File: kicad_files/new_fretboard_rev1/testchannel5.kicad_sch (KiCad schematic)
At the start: 22 parts, among them U2 LX3302AQPW-TR-EASY

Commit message: got 6 of em
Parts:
- removed C12, C13: 680pf, Capacitor_SMD:C_0603_1608Metric, symbol Device:C
- removed C14, C15: 10pf, Capacitor_SMD:C_0402_1005Metric, symbol Device:C
- removed C16: 1uf, Capacitor_SMD:C_0603_1608Metric, symbol Device:C
- removed C17, C20: 100nf, Capacitor_SMD:C_0402_1005Metric, symbol Device:C
- removed C18, C19: 6.8nf, Capacitor_SMD:C_0402_1005Metric, symbol Device:C
- removed C21: 1000pf, Capacitor_SMD:C_0402_1005Metric, symbol Device:C
- removed C22: 470nf, Capacitor_SMD:C_0402_1005Metric, symbol Device:C
- removed L5, L6, L7, L8: L, NetTie:NetTie-2_SMD_Pad0.5mm, symbol Device:L
- removed R10, R11, R8, R9: 10R, Resistor_SMD:R_0402_1005Metric, symbol Device:R
- removed R12: 221R, Resistor_SMD:R_0402_1005Metric, symbol Device:R
- removed R13: 4.7R, Resistor_SMD:R_0402_1005Metric, symbol Device:R
- removed U2: LX3302AQPW-TR-EASY, Snapeda:14-TSSOP_MCH-L, symbol Snapeda:LX3302AQPW-TR-EASY
- added C56, C62: 100nf, Capacitor_SMD:C_0402_1005Metric, symbol Device:C
- added C57: 1000pf, Capacitor_SMD:C_0402_1005Metric, symbol Device:C
- added C58: 470nf, Capacitor_SMD:C_0402_1005Metric, symbol Device:C
- added C59: 1uf, Capacitor_SMD:C_0603_1608Metric, symbol Device:C
- added C60, C61: 6.8nf, Capacitor_SMD:C_0402_1005Metric, symbol Device:C
- added C63, C64: 10pf, Capacitor_SMD:C_0402_1005Metric, symbol Device:C
- added C65, C66: 680pf, Capacitor_SMD:C_0603_1608Metric, symbol Device:C
- added L21, L22, L23, L24: L, NetTie:NetTie-2_SMD_Pad0.5mm, symbol Device:L
- added R31: 4.7R, Resistor_SMD:R_0402_1005Metric, symbol Device:R
- added R32: 221R, Resistor_SMD:R_0402_1005Metric, symbol Device:R
- added R33, R34, R35, R36: 10R, Resistor_SMD:R_0402_1005Metric, symbol Device:R
- added U6: LX3302AQPW-TR-EASY, Snapeda:14-TSSOP_MCH-L, symbol Snapeda:LX3302AQPW-TR-EASY
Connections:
- net CL1B_A: now also L24.1, R36.2
- net CL1_A: now also C63.1, R36.1, U6.8 (CL1)
- net CL2B_A: now also L23.1, R35.2
- net CL2_A: now also C64.1, R35.1, U6.10 (CL2)
- net GND: now also C56.1, C57.1, C58.1, C59.1, C60.1, C61.1, C63.2, C64.2, C65.2, C66.2, L23.2, L24.2, U6.2 (GND), U6.9 (GNDCL)
- net OSC11_A: now also C65.1, L21.2, U6.13 (OSC1)
- net OSC12_A: now also C66.1, L22.2, U6.12 (OSC2)
- net SUB_A: now also C62.1, U6.11 (SUB)
- net VIN_A: now also C57.2, C58.2, R31.1, R33.2, R34.1, U6.4 (VIN)
- new net: C60.2, R32.2
- new net: C61.2, R32.1, R33.1, U6.6 (IO2)
- new net: C56.2, R31.2
- new net: C59.2, C62.2, U6.5 (VDD)
- new net /OSC2B_A: L21.1, L22.1, R34.2
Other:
- removed sheet testchannel1
- removed sheet testchannel2
- removed sheet testchannel3
- removed sheet testchannel4
- removed sheet testchannel5

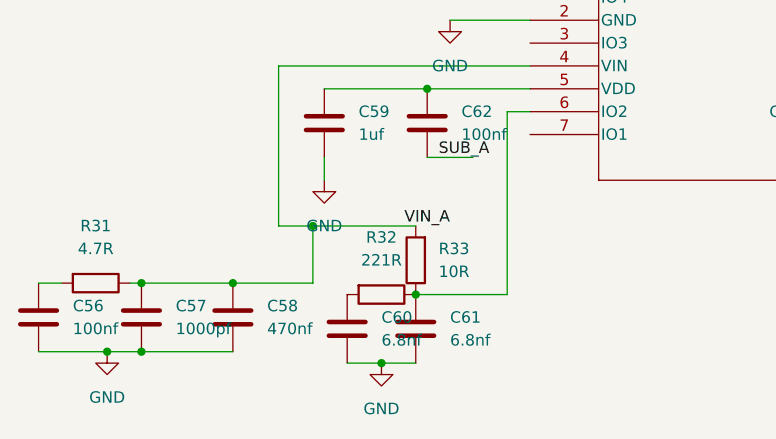
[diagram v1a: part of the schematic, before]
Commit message: stm32 micro added
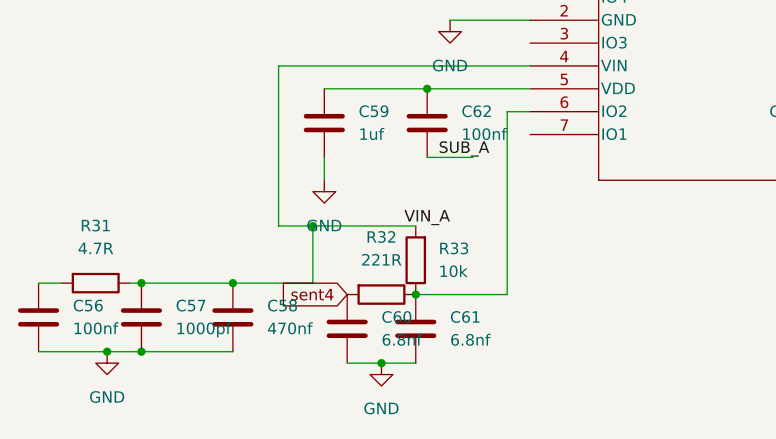
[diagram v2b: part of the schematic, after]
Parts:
- R33: value 10R -> 10k
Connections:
- net sent4: now reaches C60.2, R32.2
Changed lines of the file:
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@@
+		)
+	)
+	(global_label "sent4"
+		(shape input)
+		(at 110.49 125.73 180)
+		(fields_autoplaced yes)
+		(effects
+			(font
+				(size 1.27 1.27)
+			)
+			(justify right)
+		)
+		(property "Intersheetrefs" "${INTERSHEET_REFS}"
+			(at 102.3039 125.73 0)
+			(effects
+				(font
+					(size 1.27 1.27)
+				)
+				(justify right)
+				(hide yes)
+			)
 		)
 	)
@@
 			)
 		)
-		(property "Component Class" ""
-			(at 184.15 57.15 0)
-			(effects
-				(font
-					(size 1.27 1.27)
-				)
-				(hide yes)
-			)
-		)
 		(pin "2"
 		)
@@
 			)
 		)
-		(property "Component Class" ""
-			(at 203.2 121.92 90)
-			(effects
-				(font
-					(size 1.27 1.27)
-				)
-				(hide yes)
-			)
-		)
 		(pin "1"
 		)
@@
 			)
 		)
-		(property "Component Class" ""
-			(at 110.49 129.54 0)
-			(effects
-				(font
-					(size 1.27 1.27)
-				)
-				(hide yes)
-			)
-		)
 		(pin "1"
 		)
@@
 			)
 		)
-		(property "Value" "10R"
+		(property "Value" "10k"
 			(at 120.65 123.1899 0)
 			(effects
@@
 			)
 		)
-		(property "Component Class" ""
-			(at 118.11 121.92 0)
-			(effects
-				(font
-					(size 1.27 1.27)
-				)
-				(hide yes)
-			)
-		)
 		(pin "2"
 		)
@@
 			)
 		)
-		(property "Component Class" ""
-			(at 114.3 125.73 90)
-			(effects
-				(font
-					(size 1.27 1.27)
-				)
-				(hide yes)
-			)
-		)
 		(pin "2"
 		)
@@
 			)
 		)
-		(property "Component Class" ""
-			(at 204.47 85.09 90)
-			(effects
-				(font
-					(size 1.27 1.27)
-				)
-				(hide yes)
-			)
-		)
 		(pin "1"
 		)
@@
 			)
 		)
-		(property "Component Class" ""
-			(at 82.55 124.46 90)
-			(effects
-				(font
-					(size 1.27 1.27)
-				)
-				(hide yes)
-			)
-		)
 		(pin "2"
 		)
@@
 			)
 		)
-		(property "Component Class" ""
-			(at 194.31 68.58 0)
-			(effects
-				(font
-					(size 1.27 1.27)
-				)
-				(hide yes)
-			)
-		)
 		(pin "1"
 		)
@@
 			)
 		)
-		(property "Component Class" ""
-			(at 189.23 133.35 90)
-			(effects
-				(font
-					(size 1.27 1.27)
-				)
-				(hide yes)
-			)
-		)
 		(pin "1"
 		)
@@
 			)
 		)
-		(property "Component Class" ""
-			(at 97.79 128.27 0)
-			(effects
-				(font
-					(size 1.27 1.27)
-				)
-				(hide yes)
-			)
-		)
 		(pin "1"
 		)
@@
 			)
 		)
-		(property "Component Class" ""
-			(at 204.47 97.79 90)
-			(effects
-				(font
-					(size 1.27 1.27)
-				)
-				(hide yes)
-			)
-		)
 		(pin "1"
 		)
@@
 			)
 		)
-		(property "Component Class" ""
-			(at 87.63 128.27 0)
-			(effects
-				(font
-					(size 1.27 1.27)
-				)
-				(hide yes)
-			)
-		)
 		(pin "1"
 		)
@@
 			)
 		)
-		(property "Component Class" ""
-			(at 76.2 128.27 0)
-			(effects
-				(font
-					(size 1.27 1.27)
-				)
-				(hide yes)
-			)
-		)
 		(pin "1"
 		)
@@
 			)
 		)
-		(property "Component Class" ""
-			(at 190.5 102.87 90)
-			(effects
-				(font
-					(size 1.27 1.27)
-				)
-				(hide yes)
-			)
-		)
 		(pin "1"
 		)
@@
 			)
 		)
-		(property "Component Class" ""
-			(at 118.11 129.54 0)
-			(effects
-				(font
-					(size 1.27 1.27)
-				)
-				(hide yes)
-			)
-		)
 		(pin "1"
 		)
@@
 			)
 		)
-		(property "Component Class" ""
-			(at 191.77 121.92 90)
-			(effects
-				(font
-					(size 1.27 1.27)
-				)
-				(hide yes)
-			)
-		)
 		(pin "2"
 		)
@@
 			)
 		)
-		(property "Component Class" ""
-			(at 119.38 106.68 0)
-			(effects
-				(font
-					(size 1.27 1.27)
-				)
-				(hide yes)
-			)
-		)
 		(pin "1"
 		)
@@
 			)
 		)
-		(property "Component Class" ""
-			(at 184.15 68.58 0)
-			(effects
-				(font
-					(size 1.27 1.27)
-				)
-				(hide yes)
-			)
-		)
 		(pin "1"
 		)
@@
 			)
 		)
-		(property "Component Class" ""
-			(at 203.2 113.03 90)
-			(effects
-				(font
-					(size 1.27 1.27)
-				)
-				(hide yes)
-			)
-		)
 		(pin "1"
 		)
@@
 			)
 		)
-		(property "Component Class" ""
-			(at 190.5 113.03 90)
-			(effects
-				(font
-					(size 1.27 1.27)
-				)
-				(hide yes)
-			)
-		)
 		(pin "2"
 		)
@@
 			)
 		)
-		(property "Component Class" ""
-			(at 130.81 92.71 0)
-			(effects
-				(font
-					(size 1.27 1.27)
-				)
-				(hide yes)
-			)
-		)
 		(pin "5"
 		)
@@
 			(at 107.95 106.68 0)
 			(effects
-				(font
-					(size 1.27 1.27)
-				)
-				(hide yes)
-			)
-		)
-		(property "Component Class" ""
-			(at 107.95 106.68 0)
-			(effects

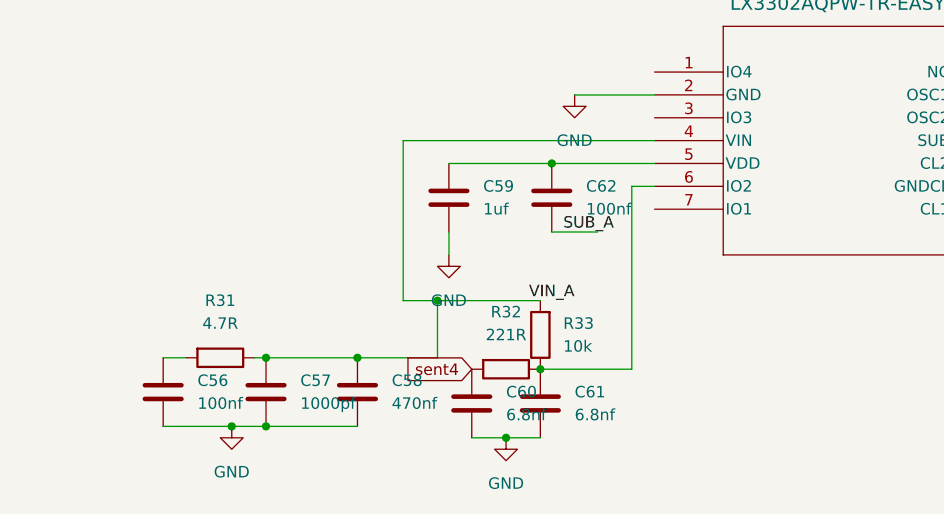
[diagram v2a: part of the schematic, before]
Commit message: mcu configured, still needs power connections and spi i2c connections
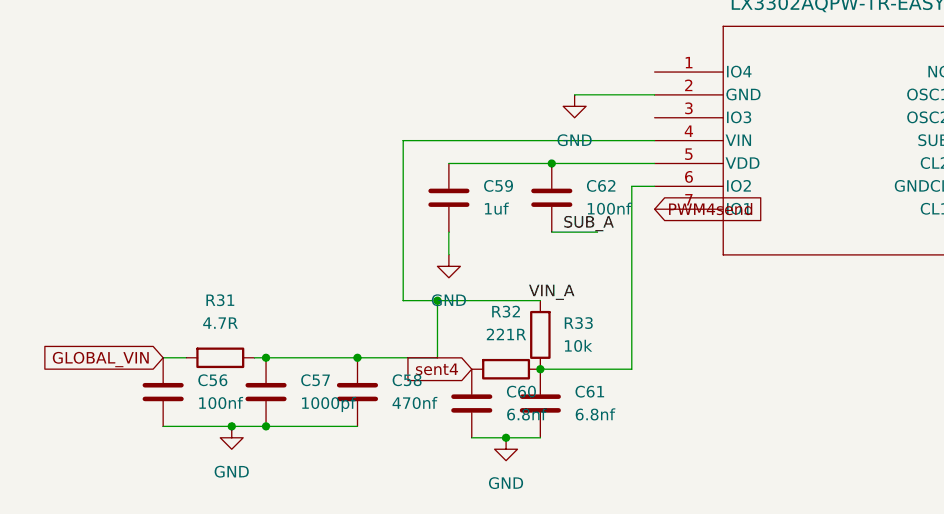
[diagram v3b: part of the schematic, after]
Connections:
- net GLOBAL_VIN: now reaches C56.2, R31.2
- net PWM4send: now reaches U6.7 (IO1)
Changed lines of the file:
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@@
+		)
+	)
+	(global_label "GLOBAL_VIN"
+		(shape input)
+		(at 76.2 124.46 180)
+		(fields_autoplaced yes)
+		(effects
+			(font
+				(size 1.27 1.27)
+			)
+			(justify right)
+		)
+		(property "Intersheetrefs" "${INTERSHEET_REFS}"
+			(at 62.208 124.46 0)
+			(effects
+				(font
+					(size 1.27 1.27)
+				)
+				(justify right)
+				(hide yes)
+			)
+		)
+	)
+	(global_label "PWM4send"
+		(shape input)
+		(at 130.81 107.95 0)
+		(fields_autoplaced yes)
+		(effects
+			(font
+				(size 1.27 1.27)
+			)
+			(justify left)
+		)
+		(property "Intersheetrefs" "${INTERSHEET_REFS}"
+			(at 143.5922 107.95 0)
+			(effects
+				(font
+					(size 1.27 1.27)
+				)
+				(justify left)
+				(hide yes)
+			)
 		)
 	)

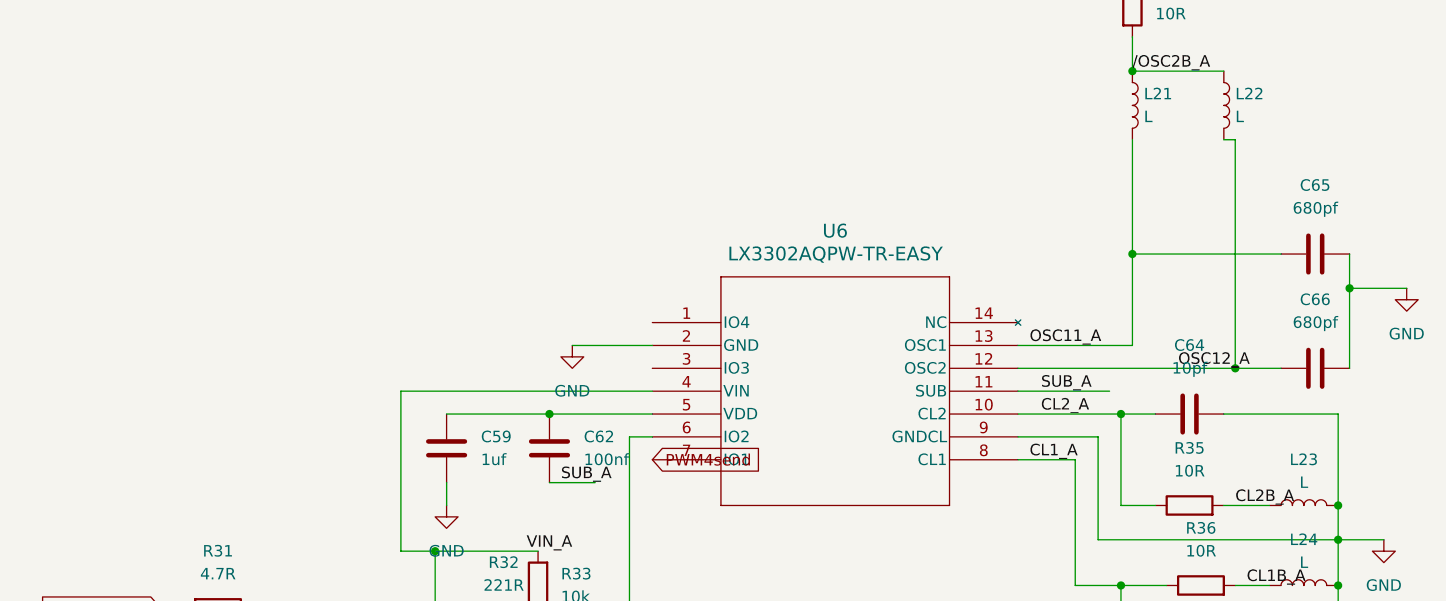
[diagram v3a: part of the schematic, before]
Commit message: finished routing - adding silkscreen
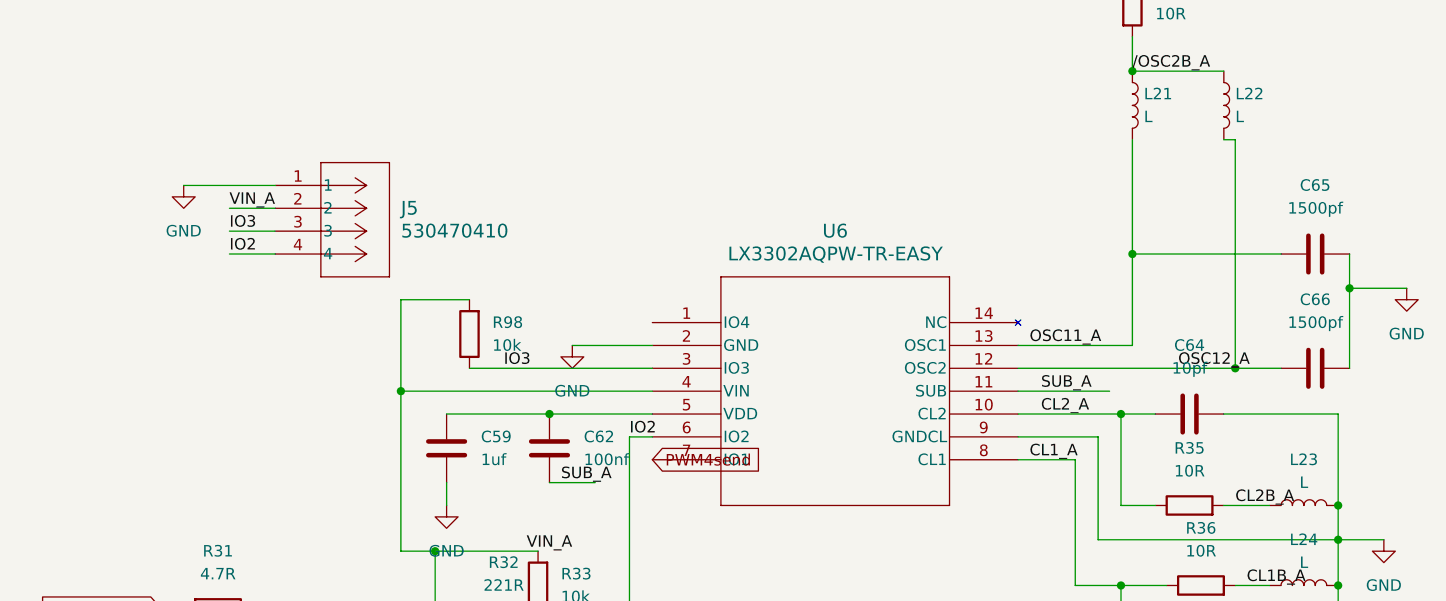
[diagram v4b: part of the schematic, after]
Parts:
- added J5: 530470410, Snapeda:CONN04_530470410_MOL, symbol Snapeda:530470410
- added R98: 10k, Resistor_SMD:R_0402_1005Metric, symbol Device:R
- C65, C66: value 680pf -> 1500pf
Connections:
- net GND: now also J5.1
- net VIN_A: now also J5.2, R98.2
- net IO2: now reaches C61.2, R32.1, R33.1, U6.6 (IO2)
- net IO2: now also J5.4
- net IO3: now reaches U6.3 (IO3)
- net IO3: now also J5.3, R98.1

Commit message: exported gerbers of lefthand
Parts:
- L21, L22, L23, L24: now left out of the parts list
